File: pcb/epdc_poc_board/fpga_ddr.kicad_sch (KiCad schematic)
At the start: 35 parts, among them U201 ECP5U_45_CABGA256, U502 MT41K256M16HA

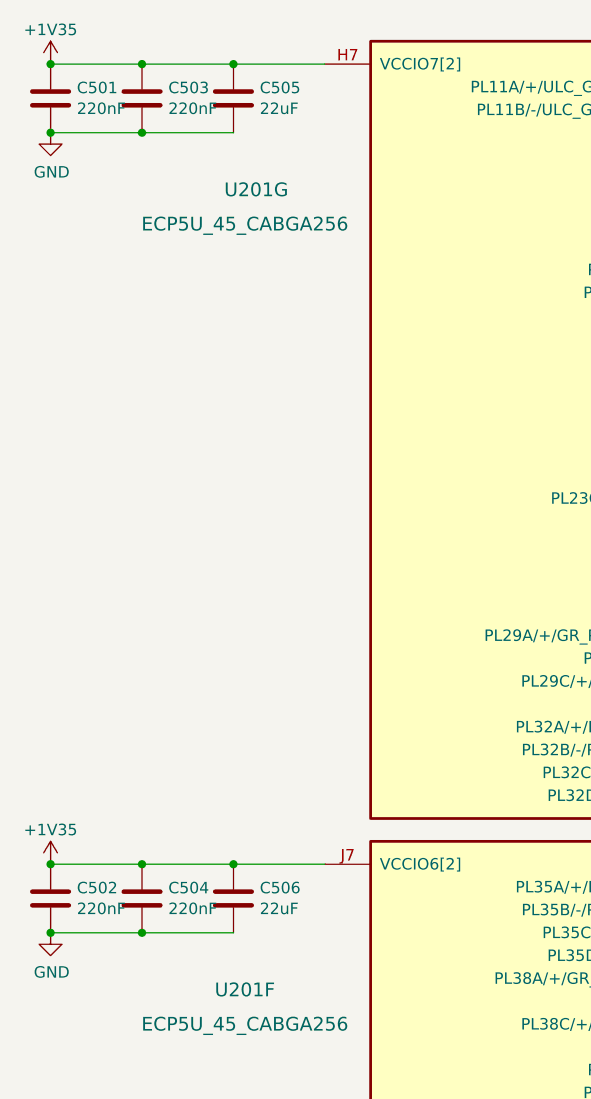
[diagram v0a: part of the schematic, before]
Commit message: - wip epdc poc board, going to remove vga input
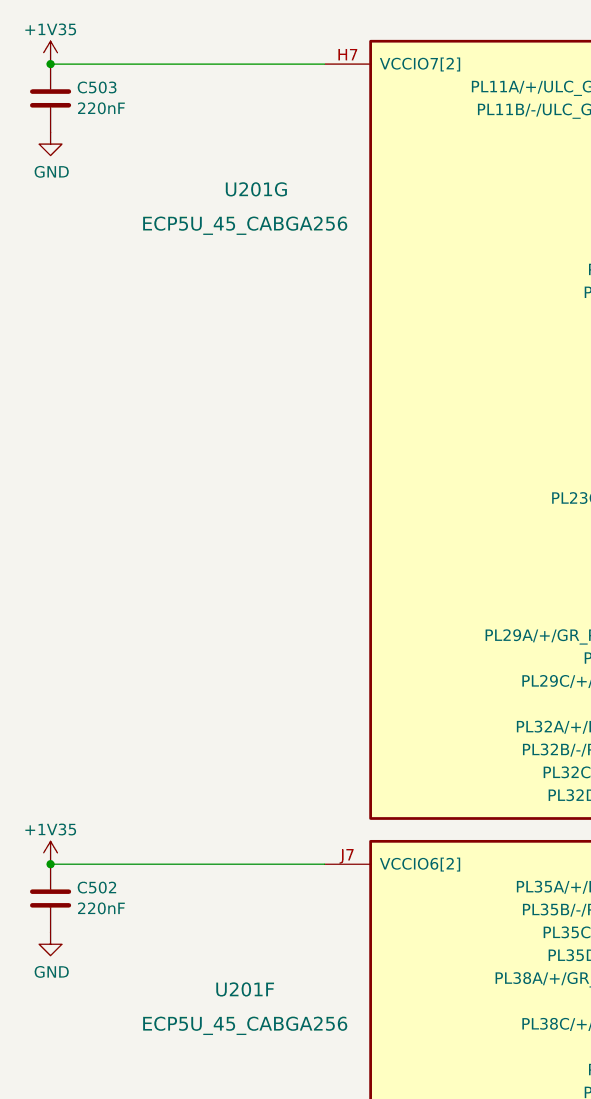
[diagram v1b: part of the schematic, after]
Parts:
- removed C501, C504: 220nF, Capacitor_SMD:C_0402_1005Metric, symbol Device:C
- removed C505, C506: 22uF, Capacitor_SMD:C_0603_1608Metric, symbol Device:C
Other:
- moved on the sheet: C503
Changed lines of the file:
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@@
   (paper "A4")
   (junction (at 21.59 20.32) (diameter 0) (color 0 0 0 0))
-  (junction (at 21.59 27.94) (diameter 0) (color 0 0 0 0))
   (junction (at 21.59 109.22) (diameter 0) (color 0 0 0 0))
-  (junction (at 21.59 116.84) (diameter 0) (color 0 0 0 0))
-  (junction (at 31.75 20.32) (diameter 0.9144) (color 0 0 0 0))
-  (junction (at 31.75 27.94) (diameter 0.9144) (color 0 0 0 0))
-  (junction (at 31.75 109.22) (diameter 0.9144) (color 0 0 0 0))
-  (junction (at 31.75 116.84) (diameter 0.9144) (color 0 0 0 0))
-  (junction (at 41.91 20.32) (diameter 0.9144) (color 0 0 0 0))
-  (junction (at 41.91 109.22) (diameter 0.9144) (color 0 0 0 0))
   (junction (at 128.27 68.58) (diameter 0) (color 0 0 0 0))
   (junction (at 128.27 144.78) (diameter 0) (color 0 0 0 0))
@@
   (junction (at 264.16 147.32) (diameter 0.9144) (color 0 0 0 0))
   (no_connect (at 201.93 39.37))
-  (wire (pts (xy 21.59 20.32) (xy 31.75 20.32))
-    (stroke (width 0) (type solid) (color 0 0 0 0))
-  )
-  (wire (pts (xy 21.59 109.22) (xy 31.75 109.22))
-    (stroke (width 0) (type solid) (color 0 0 0 0))
-  )
-  (wire (pts (xy 31.75 20.32) (xy 41.91 20.32))
-    (stroke (width 0) (type solid) (color 0 0 0 0))
-  )
-  (wire (pts (xy 31.75 27.94) (xy 21.59 27.94))
-    (stroke (width 0) (type solid) (color 0 0 0 0))
-  )
-  (wire (pts (xy 31.75 109.22) (xy 41.91 109.22))
-    (stroke (width 0) (type solid) (color 0 0 0 0))
-  )
-  (wire (pts (xy 31.75 116.84) (xy 21.59 116.84))
-    (stroke (width 0) (type solid) (color 0 0 0 0))
-  )
-  (wire (pts (xy 41.91 20.32) (xy 52.07 20.32))
-    (stroke (width 0) (type solid) (color 0 0 0 0))
-  )
-  (wire (pts (xy 41.91 27.94) (xy 31.75 27.94))
-    (stroke (width 0) (type solid) (color 0 0 0 0))
-  )
-  (wire (pts (xy 41.91 109.22) (xy 52.07 109.22))
-    (stroke (width 0) (type solid) (color 0 0 0 0))
-  )
-  (wire (pts (xy 41.91 116.84) (xy 31.75 116.84))
+  (wire (pts (xy 21.59 20.32) (xy 52.07 20.32))
+    (stroke (width 0) (type solid) (color 0 0 0 0))
+  )
+  (wire (pts (xy 21.59 109.22) (xy 52.07 109.22))
     (stroke (width 0) (type solid) (color 0 0 0 0))
   )
@@
   (symbol (lib_id "Device:C") (at 21.59 24.13 0) (unit 1)
     (in_bom yes) (on_board yes)
-    (property "Reference" "C501" (id 0) (at 24.511 22.9616 0)
+    (property "Reference" "C503" (id 0) (at 24.511 22.9616 0)
       (effects (font (size 1.27 1.27)) (justify left))
     )
@@
       (effects (font (size 1.27 1.27)) hide)
     )
-    (pin "1")
-    (pin "2")
-  )
-  (symbol (lib_id "Device:C") (at 31.75 24.13 0) (unit 1)
-    (in_bom yes) (on_board yes)
-    (property "Reference" "C503" (id 0) (at 34.671 22.9616 0)
-      (effects (font (size 1.27 1.27)) (justify left))
-    )
-    (property "Value" "220nF" (id 1) (at 34.671 25.273 0)
-      (effects (font (size 1.27 1.27)) (justify left))
-    )
-    (property "Footprint" "Capacitor_SMD:C_0402_1005Metric" (id 2) (at 32.7152 27.94 0)
-      (effects (font (size 1.27 1.27)) hide)
-    )
-    (property "Datasheet" "~" (id 3) (at 31.75 24.13 0)
-      (effects (font (size 1.27 1.27)) hide)
-    )
-    (pin "1")
-    (pin "2")
-  )
-  (symbol (lib_id "Device:C") (at 31.75 113.03 0) (unit 1)
-    (in_bom yes) (on_board yes)
-    (property "Reference" "C504" (id 0) (at 34.671 111.8616 0)
-      (effects (font (size 1.27 1.27)) (justify left))
-    )
-    (property "Value" "220nF" (id 1) (at 34.671 114.173 0)
-      (effects (font (size 1.27 1.27)) (justify left))
-    )
-    (property "Footprint" "Capacitor_SMD:C_0402_1005Metric" (id 2) (at 32.7152 116.84 0)
-      (effects (font (size 1.27 1.27)) hide)
-    )
-    (property "Datasheet" "~" (id 3) (at 31.75 113.03 0)
-      (effects (font (size 1.27 1.27)) hide)
-    )
-    (pin "1")
-    (pin "2")
-  )
-  (symbol (lib_id "Device:C") (at 41.91 24.13 0) (unit 1)
-    (in_bom yes) (on_board yes)
-    (property "Reference" "C505" (id 0) (at 44.831 22.9616 0)
-      (effects (font (size 1.27 1.27)) (justify left))
-    )
-    (property "Value" "22uF" (id 1) (at 44.831 25.273 0)
-      (effects (font (size 1.27 1.27)) (justify left))
-    )
-    (property "Footprint" "Capacitor_SMD:C_0603_1608Metric" (id 2) (at 42.8752 27.94 0)
-      (effects (font (size 1.27 1.27)) hide)
-    )
-    (property "Datasheet" "~" (id 3) (at 41.91 24.13 0)
-      (effects (font (size 1.27 1.27)) hide)
-    )
-    (pin "1")
-    (pin "2")
-  )
-  (symbol (lib_id "Device:C") (at 41.91 113.03 0) (unit 1)
-    (in_bom yes) (on_board yes)
-    (property "Reference" "C506" (id 0) (at 44.831 111.8616 0)
-      (effects (font (size 1.27 1.27)) (justify left))
-    )
-    (property "Value" "22uF" (id 1) (at 44.831 114.173 0)
-      (effects (font (size 1.27 1.27)) (justify left))
-    )
-    (property "Footprint" "Capacitor_SMD:C_0603_1608Metric" (id 2) (at 42.8752 116.84 0)
-      (effects (font (size 1.27 1.27)) hide)
-    )
-    (property "Datasheet" "~" (id 3) (at 41.91 113.03 0)
-      (effects (font (size 1.27 1.27)) hide)
-    )

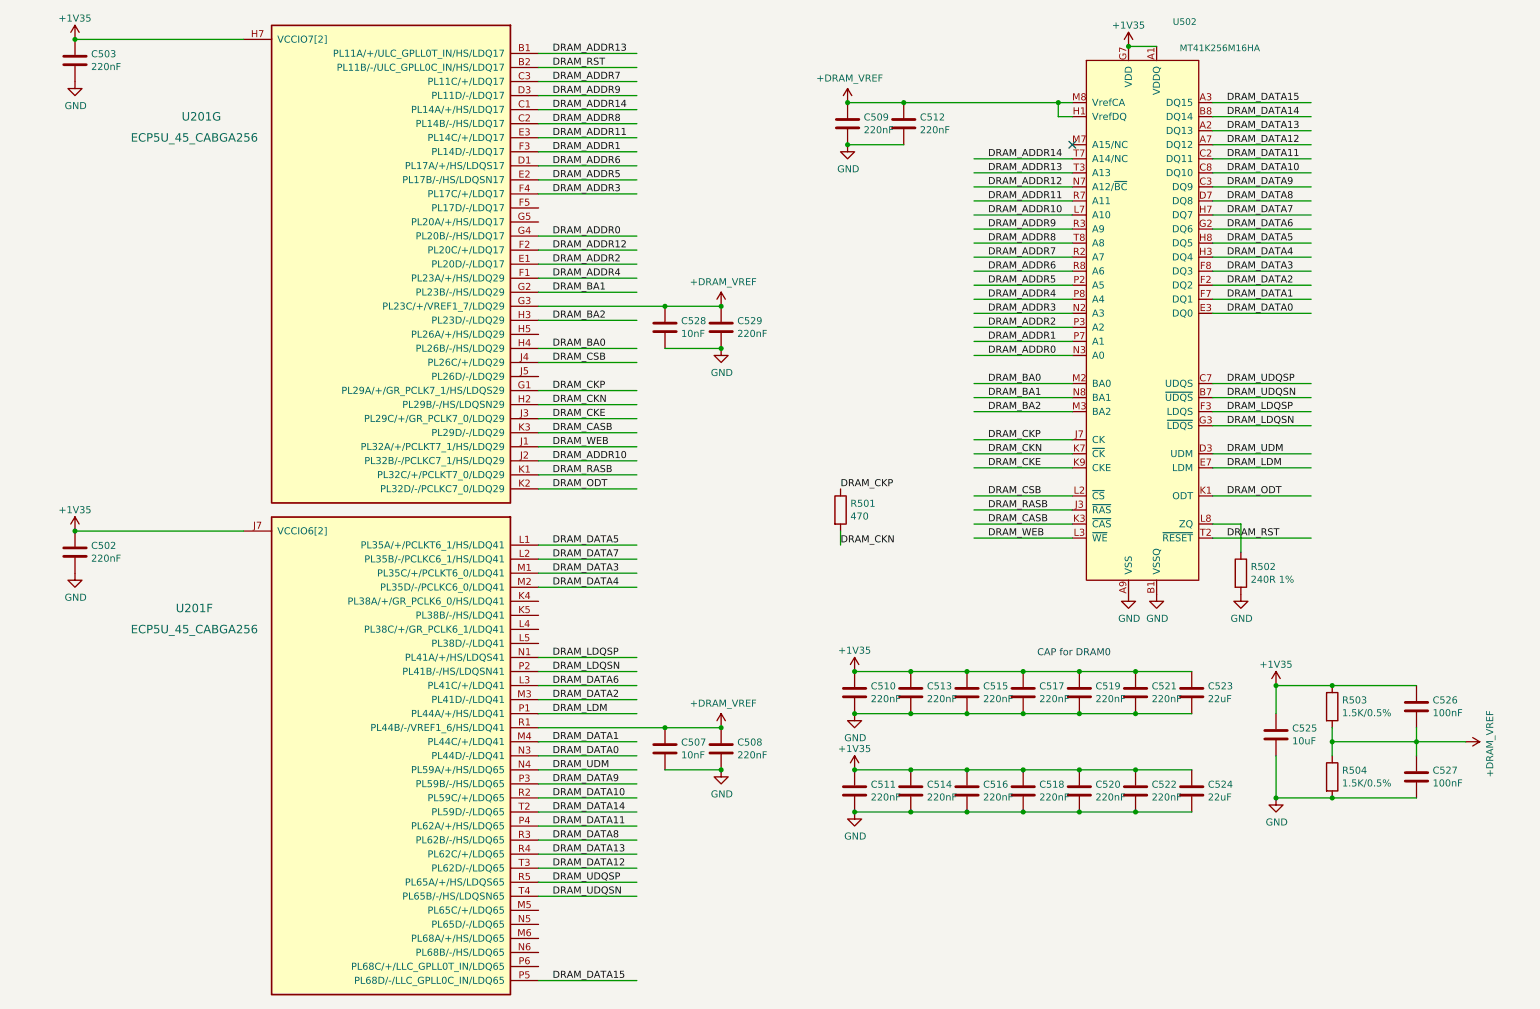
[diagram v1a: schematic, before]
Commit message: pcb: switch to s6 for epdc board
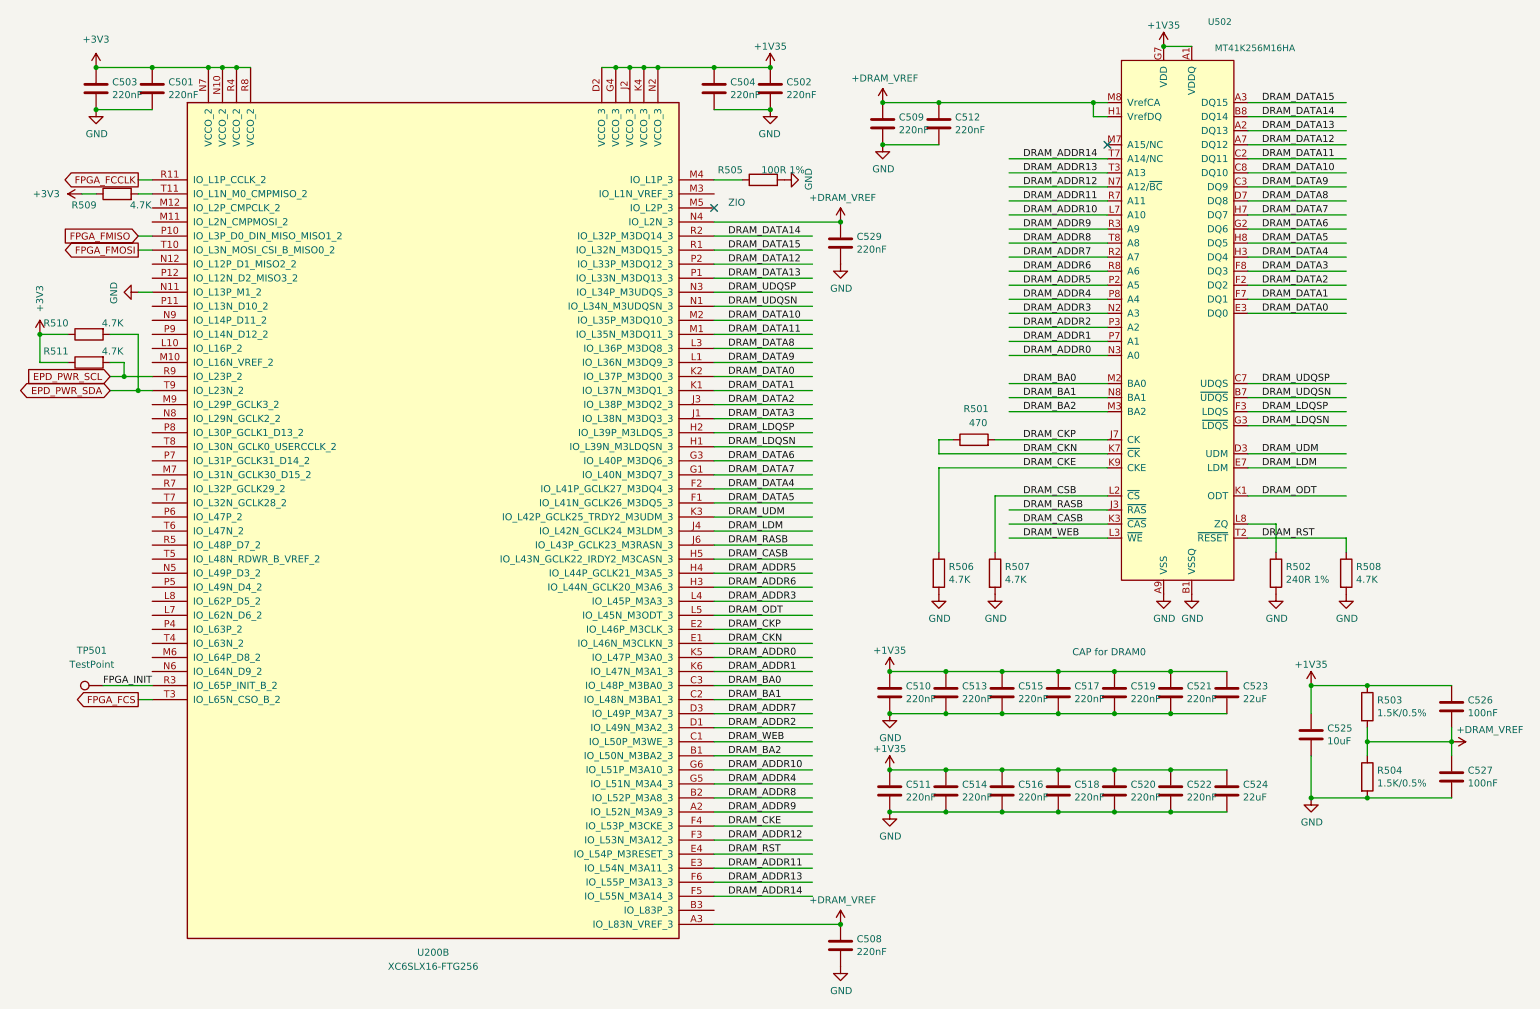
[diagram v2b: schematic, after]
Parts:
- removed C507, C528: 10nF, Capacitor_SMD:C_0402_1005Metric, symbol Device:C
- removed U201: ECP5U_45_CABGA256, Package_BGA:BGA-256_14.0x14.0mm_Layout16x16_P0.8mm_Ball0.45mm_Pad0.32mm_NSMD, symbol symbols:ECP5U_45_CABGA256
- added C501, C504: 220nF, Capacitor_SMD:C_0402_1005Metric, symbol Device:C
- added R505: 100R 1%, Resistor_SMD:R_0402_1005Metric, symbol Device:R
- added R506, R507, R508, R509, R510, R511: 4.7K, Resistor_SMD:R_0402_1005Metric, symbol Device:R
- added TP501: TestPoint, TestPoint:TestPoint_Pad_D1.0mm, symbol Connector:TestPoint
- added U200: XC6SLX16-FTG256, Package_BGA:BGA-256_14.0x14.0mm_Layout16x16_P0.8mm_Ball0.45mm_Pad0.32mm_NSMD, symbol FPGA_Xilinx_Spartan6:XC6SLX16-FTG256
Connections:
- net +1V35: now also C504.1, U200.D2 (VCCO_3), U200.G4 (VCCO_3), U200.J2 (VCCO_3), U200.K4 (VCCO_3), U200.N2 (VCCO_3); no longer C503.1
- net +DRAM_VREF: now also U200.A3 (IO_L83N_VREF_3), U200.N4 (IO_L2N_3)
- net DRAM_ADDR0: now also U200.K5 (IO_L47P_M3A0_3)
- net DRAM_ADDR1: now also U200.K6 (IO_L47N_M3A1_3)
- net DRAM_ADDR10: now also U200.G6 (IO_L51P_M3A10_3)
- net DRAM_ADDR11: now also U200.E3 (IO_L54N_M3A11_3)
- net DRAM_ADDR12: now also U200.F3 (IO_L53N_M3A12_3)
- net DRAM_ADDR13: now also U200.F6 (IO_L55P_M3A13_3)
- net DRAM_ADDR14: now also U200.F5 (IO_L55N_M3A14_3)
- net DRAM_ADDR2: now also U200.D1 (IO_L49N_M3A2_3)
- net DRAM_ADDR3: now also U200.L4 (IO_L45P_M3A3_3)
- net DRAM_ADDR4: now also U200.G5 (IO_L51N_M3A4_3)
- net DRAM_ADDR5: now also U200.H4 (IO_L44P_GCLK21_M3A5_3)
- net DRAM_ADDR6: now also U200.H3 (IO_L44N_GCLK20_M3A6_3)
- net DRAM_ADDR7: now also U200.D3 (IO_L49P_M3A7_3)
- net DRAM_ADDR8: now also U200.B2 (IO_L52P_M3A8_3)
- net DRAM_ADDR9: now also U200.A2 (IO_L52N_M3A9_3)
- net DRAM_BA0: now also U200.C3 (IO_L48P_M3BA0_3)
- net DRAM_BA1: now also U200.C2 (IO_L48N_M3BA1_3)
- net DRAM_BA2: now also U200.B1 (IO_L50N_M3BA2_3)
- net DRAM_CASB: now also U200.H5 (IO_L43N_GCLK22_IRDY2_M3CASN_3)
- net DRAM_CKE: now also R506.1, U200.F4 (IO_L53P_M3CKE_3)
- net DRAM_CKN: now also R501.1, U200.E1 (IO_L46N_M3CLKN_3); no longer R501.2
- net DRAM_CKP: now also R501.2, U200.E2 (IO_L46P_M3CLK_3); no longer R501.1
- net DRAM_CSB: now also R507.1
- net DRAM_DATA0: now also U200.K2 (IO_L37P_M3DQ0_3)
- net DRAM_DATA1: now also U200.K1 (IO_L37N_M3DQ1_3)
- net DRAM_DATA10: now also U200.M2 (IO_L35P_M3DQ10_3)
- net DRAM_DATA11: now also U200.M1 (IO_L35N_M3DQ11_3)
- net DRAM_DATA12: now also U200.P2 (IO_L33P_M3DQ12_3)
- net DRAM_DATA13: now also U200.P1 (IO_L33N_M3DQ13_3)
- net DRAM_DATA14: now also U200.R2 (IO_L32P_M3DQ14_3)
- net DRAM_DATA15: now also U200.R1 (IO_L32N_M3DQ15_3)
- net DRAM_DATA2: now also U200.J3 (IO_L38P_M3DQ2_3)
- net DRAM_DATA3: now also U200.J1 (IO_L38N_M3DQ3_3)
- net DRAM_DATA4: now also U200.F2 (IO_L41P_GCLK27_M3DQ4_3)
- net DRAM_DATA5: now also U200.F1 (IO_L41N_GCLK26_M3DQ5_3)
- net DRAM_DATA6: now also U200.G3 (IO_L40P_M3DQ6_3)
- net DRAM_DATA7: now also U200.G1 (IO_L40N_M3DQ7_3)
- net DRAM_DATA8: now also U200.L3 (IO_L36P_M3DQ8_3)
- net DRAM_DATA9: now also U200.L1 (IO_L36N_M3DQ9_3)
- net DRAM_LDM: now also U200.J4 (IO_L42N_GCLK24_M3LDM_3)
- net DRAM_LDQSN: now also U200.H1 (IO_L39N_M3LDQSN_3)
- net DRAM_LDQSP: now also U200.H2 (IO_L39P_M3LDQS_3)
- net DRAM_ODT: now also U200.L5 (IO_L45N_M3ODT_3)
- net DRAM_RASB: now also U200.J6 (IO_L43P_GCLK23_M3RASN_3)
- net DRAM_RST: now also R508.1, U200.E4 (IO_L54P_M3RESET_3)
- net DRAM_UDM: now also U200.K3 (IO_L42P_GCLK25_TRDY2_M3UDM_3)
- net DRAM_UDQSN: now also U200.N1 (IO_L34N_M3UDQSN_3)
- net DRAM_UDQSP: now also U200.N3 (IO_L34P_M3UDQS_3)
- net DRAM_WEB: now also U200.C1 (IO_L50P_M3WE_3)
- net GND: now also C501.2, C504.2, R505.2, R506.2, R507.2, R508.2, U200.N11 (IO_L13P_M1_2)
- new net: R509.2, U200.T11 (IO_L1N_M0_CMPMISO_2)
- new net: R505.1, U200.M4 (IO_L1P_3)
- new net +3V3: C501.1, C503.1, R509.1, R510.1, R511.1, U200.N10 (VCCO_2), U200.N7 (VCCO_2), U200.R4 (VCCO_2), U200.R8 (VCCO_2)
- new net EPD_PWR_SCL: R511.2, U200.R9 (IO_L23P_2)
- new net EPD_PWR_SDA: R510.2, U200.T9 (IO_L23N_2)
- new net FPGA_FCCLK: U200.R11 (IO_L1P_CCLK_2)
- new net FPGA_FCS: U200.T3 (IO_L65N_CSO_B_2)
- new net FPGA_FMISO: U200.P10 (IO_L3P_D0_DIN_MISO_MISO1_2)
- new net FPGA_FMOSI: U200.T10 (IO_L3N_MOSI_CSI_B_MISO0_2)
- new net FPGA_INIT: TP501.1, U200.R3 (IO_L65P_INIT_B_2)
- no-connect marks 1 -> 2
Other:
- note added: "ZIO"
- moved on the sheet: C502, C503, C508, C509, C510, C511, C512, C513, C514, C515, C516, C517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

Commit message: pcb: mb r0.1, caster r0.1 freeze
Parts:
- C501, C502, C503, C504, C508, C509, C510, C511, C512, C513, C514, C515, C516, C517, C518, C519, C520, C521, C522, C529: LCSC (none) -> C880414; Ref.Price (none) -> 0.0036
- C523, C524: LCSC (none) -> C94018; Ref.Price (none) -> 0.0301
- C525: LCSC (none) -> C105490; Ref.Price (none) -> 0.0165
- C526, C527: LCSC (none) -> C56392; Ref.Price (none) -> 0.0023
- R501: value 470 -> 470R; LCSC (none) -> C114877; Ref.Price (none) -> 0.001
- R502: value 240R 1% -> 240R/1%; LCSC (none) -> C114755; Ref.Price (none) -> 0.0009
- R503, R504: LCSC (none) -> C226693; Ref.Price (none) -> 0.0025
- R505: LCSC (none) -> C106232; Ref.Price (none) -> 0.0007
- R506, R507, R508, R509, R510, R511: LCSC (none) -> C105870; Ref.Price (none) -> 0.0006
- TP501: LCSC (none) -> -; Ref.Price (none) -> 0
- U200: LCSC (none) -> C39313; Ref.Price (none) -> 7.4837
- U502: value MT41K256M16HA -> MT41K64M16TW; LCSC (none) -> C524855; Ref.Price (none) -> 3.2405
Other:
- company: (none) -> Copyright 2021 Modos / Engineer: Wenting Zhang
- title: (none) -> Caster EPDC
